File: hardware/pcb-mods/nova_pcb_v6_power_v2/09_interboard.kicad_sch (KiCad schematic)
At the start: 1 part, among them J20 IB_2x06

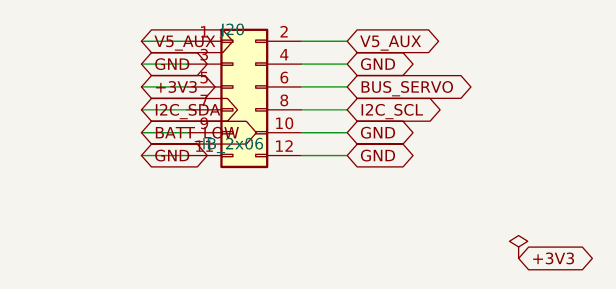
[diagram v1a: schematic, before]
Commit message: power board: fix reversed XT connector polarity (all 9 AMASS XT)
AMASS XT footprints number pad1=chamfer/NEGATIVE, pad2=flat/POSITIVE.
Board had +V wired to pad1 -> every keyed power connector reverse-wired:
J1 (XT60 battery in), J3-J7 (rail injection), J12-J14 (Jetson/L2/arm out).
Mating a normally-built cable would feed +V to the - terminal and fry the
connected load (Jetson, servos, arm). Confirmed against footprint flat/chamfer
geometry + physical connector (flat=+).

Fix: swapped pin1/pin2 net assignment on all 9 connectors in schematic,
re-routed PCB, regenerated 14-file gerber set. Pololu bucks use a custom
non-keyed terminal (pad1=rect=+V) and were correctly left unchanged.

Verify: ERC 0, DRC 0 hard / 0 unconnected, fab_gate GO, J20 match intact.

Co-Authored-By: Claude Opus 4.8 <noreply@anthropic.com>
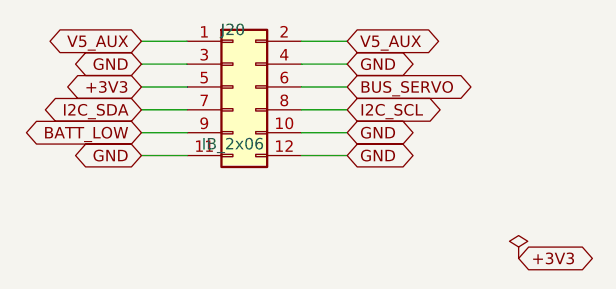
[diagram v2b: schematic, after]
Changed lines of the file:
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@@
 	(global_label "I2C_SDA"
 		(shape bidirectional)
-		(at 138.43 104.14 0)
-		(effects
-			(font
-				(size 1.27 1.27)
-			)
-			(justify left)
+		(at 138.43 104.14 180)
+		(effects
+			(font
+				(size 1.27 1.27)
+			)
+			(justify right)
 		)
 		(property "Intersheetrefs" "${INTERSHEET_REFS}"
@@
 	(global_label "V5_AUX"
 		(shape bidirectional)
-		(at 138.43 96.52 0)
-		(effects
-			(font
-				(size 1.27 1.27)
-			)
-			(justify left)
+		(at 138.43 96.52 180)
+		(effects
+			(font
+				(size 1.27 1.27)
+			)
+			(justify right)
 		)
 		(property "Intersheetrefs" "${INTERSHEET_REFS}"
@@
 	(global_label "BATT_LOW"
 		(shape bidirectional)
-		(at 138.43 106.68 0)
-		(effects
-			(font
-				(size 1.27 1.27)
-			)
-			(justify left)
+		(at 138.43 106.68 180)
+		(effects
+			(font
+				(size 1.27 1.27)
+			)
+			(justify right)
 		)
 		(property "Intersheetrefs" "${INTERSHEET_REFS}"
@@
 	(global_label "GND"
 		(shape bidirectional)
-		(at 138.43 99.06 0)
-		(effects
-			(font
-				(size 1.27 1.27)
-			)
-			(justify left)
+		(at 138.43 99.06 180)
+		(effects
+			(font
+				(size 1.27 1.27)
+			)
+			(justify right)
 		)
 		(property "Intersheetrefs" "${INTERSHEET_REFS}"
@@
 	(global_label "+3V3"
 		(shape bidirectional)
-		(at 138.43 101.6 0)
-		(effects
-			(font
-				(size 1.27 1.27)
-			)
-			(justify left)
+		(at 138.43 101.6 180)
+		(effects
+			(font
+				(size 1.27 1.27)
+			)
+			(justify right)
 		)
 		(property "Intersheetrefs" "${INTERSHEET_REFS}"
@@
 	(global_label "GND"
 		(shape bidirectional)
-		(at 138.43 109.22 0)
-		(effects
-			(font
-				(size 1.27 1.27)
-			)
-			(justify left)
-		)
-		(property "Intersheetrefs" "${INTERSHEET_REFS}"
+		(at 138.43 109.22 180)
+		(effects
+			(font
+				(size 1.27 1.27)
+			)
+			(justify right)
+		)
+		(property "Intersheetrefs" "${INTERSHEET_REFS}"
